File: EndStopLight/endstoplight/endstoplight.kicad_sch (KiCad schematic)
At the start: 8 parts

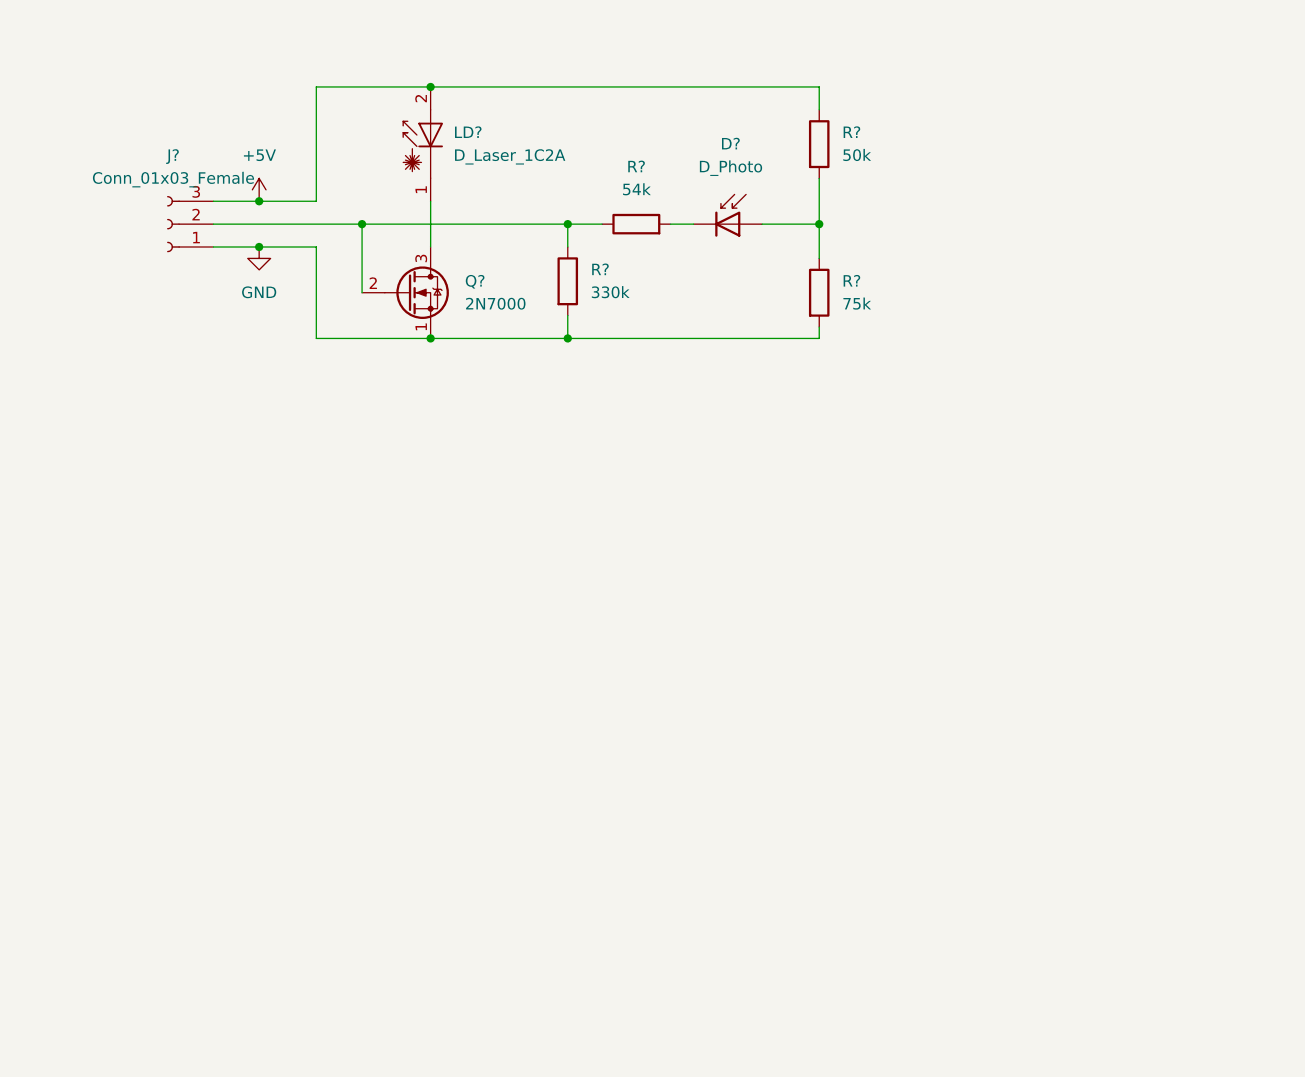
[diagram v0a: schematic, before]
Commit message: Working laser beam endstop
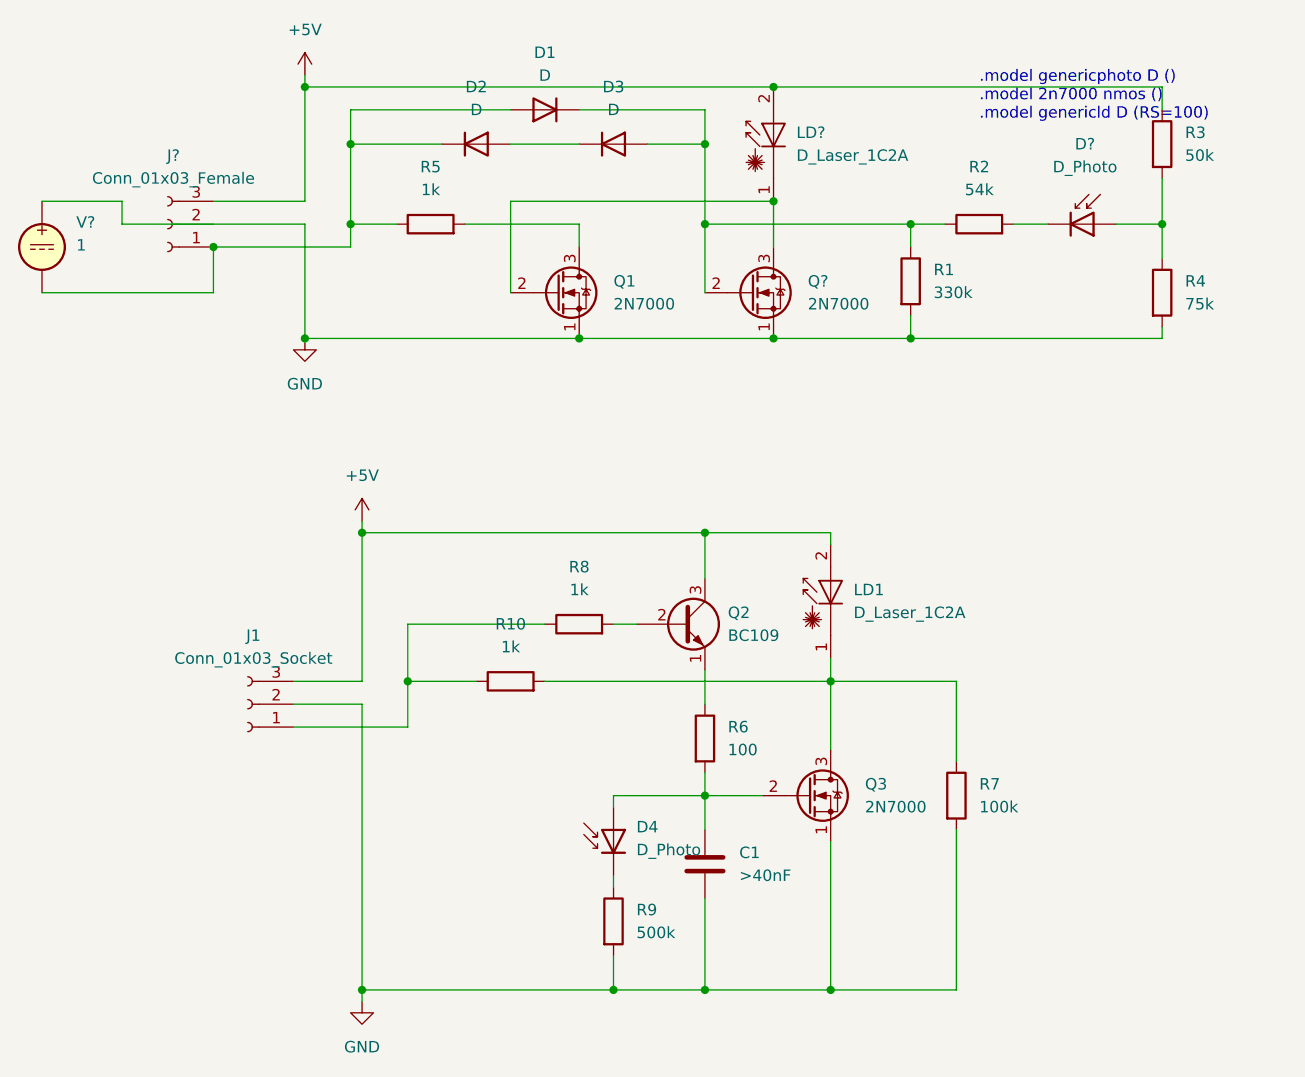
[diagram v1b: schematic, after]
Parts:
- added C1: >40nF, symbol Device:C
- added D1, D2, D3: D, symbol Device:D
- added D4: D_Photo, symbol Device:D_Photo
- added J1: Conn_01x03_Socket, symbol Connector:Conn_01x03_Socket
- added LD1: D_Laser_1C2A, symbol Device:D_Laser_1C2A
- added Q1, Q3: 2N7000, Package_TO_SOT_THT:TO-92_Inline, symbol Transistor_FET:2N7000
- added Q2: BC109, Package_TO_SOT_THT:TO-18-3, symbol Transistor_BJT:BC109
- added R10, R5, R8: 1k, symbol Device:R
- added R6: 100, symbol Device:R
- added R7: 100k, symbol Device:R
- added R9: 500k, symbol Device:R
- added V?: 1, symbol Simulation_SPICE:VDC
- gave numbers to parts that had none: 4
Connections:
- net +5V: now also J1.3 (Pin_3), LD1.2 (A), Q2.3 (C)
- net GND: now also C1.2, J1.2 (Pin_2), Q1.1 (S), Q3.1 (S), R7.2, R9.2, V?.1; no longer J?.1 (Pin_1)
- net at LD?.1 (K), Q?.3 (D): now also Q1.2 (G)
- net at Q?.2 (G), R1.1, R2.1: now also D1.1 (K), D3.2 (A); no longer J?.2 (Pin_2)
- new net: J1.1 (Pin_1), R10.1, R8.1
- new net: LD1.1 (K), Q3.3 (D), R10.2, R7.1
- new net: D4.1 (K), R9.1
- new net: Q1.3 (D), R5.2
- new net: D1.2 (A), D2.1 (K), J?.1 (Pin_1), R5.1, V?.2
- new net: D2.2 (A), D3.1 (K)
- new net: Q2.2 (B), R8.2
- new net: C1.1, D4.2 (A), Q3.2 (G), R6.2
- new net: Q2.1 (E), R6.1
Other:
- note added: ".model genericphoto D () .model 2n7000 nmos () .model genericld D (RS=100)"
- moved on the sheet: D?, LD?, Q?, R1, R2, R3, R4
